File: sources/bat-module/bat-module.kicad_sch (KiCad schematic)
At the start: 31 parts, among them IC1 FDS6898AZ, IC2 DS2777G+

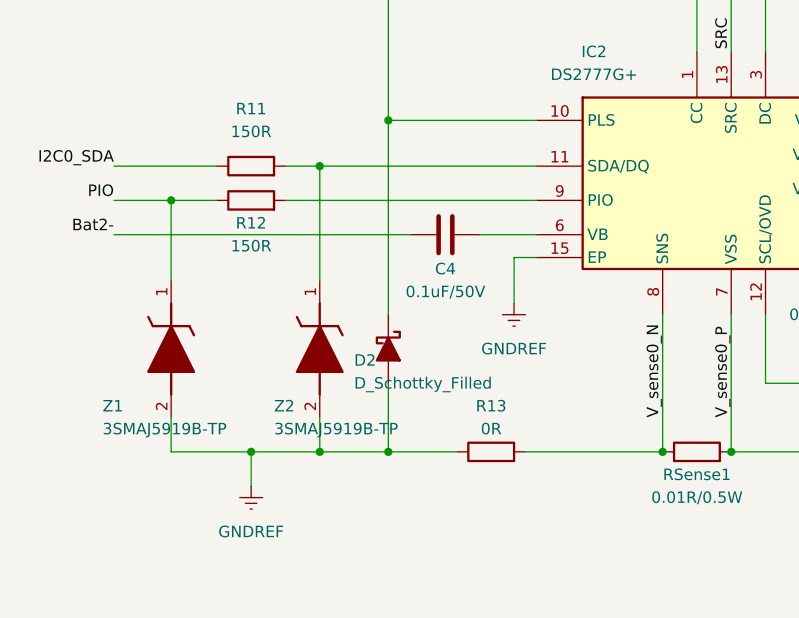
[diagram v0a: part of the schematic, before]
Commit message: hardware: creating batteries circuit
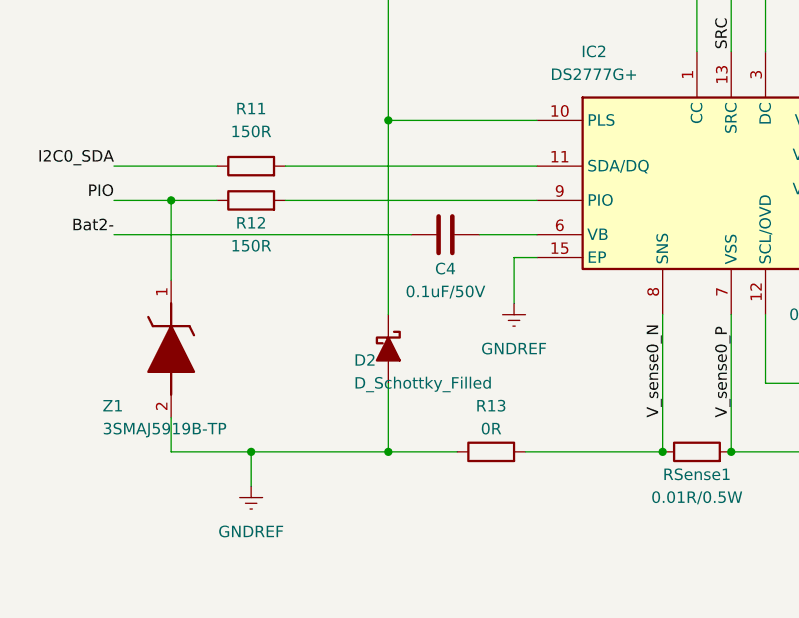
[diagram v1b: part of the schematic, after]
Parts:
- removed Z2: 3SMAJ5919B-TP, DIOM5226X244N, symbol 3SMAJ5919B-TP:3SMAJ5919B-TP
- IC1: footprint SOIC127P600X175-8N -> (none)
- IC2: footprint SON40P500X300X80-15N-D -> (none)
- Z1: footprint DIOM5226X244N -> (none)
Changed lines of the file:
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@@
   (junction (at 78.74 78.74) (diameter 0) (color 0 0 0 0)
   )
-  (junction (at 50.8 163.83) (diameter 0) (color 0 0 0 0)
-  )
   (junction (at 114.3 78.74) (diameter 0) (color 0 0 0 0)
   )
@@
   (junction (at 129.54 78.74) (diameter 0) (color 0 0 0 0)
   )
-  (junction (at 50.8 132.08) (diameter 0) (color 0 0 0 0)
-  )
   (junction (at 92.71 97.79) (diameter 0) (color 0 0 0 0)
   )
@@
     (stroke (width 0) (type default))
   )
-  (wire (pts (xy 58.42 163.83) (xy 50.8 163.83))
-    (stroke (width 0) (type default))
-  )
   (wire (pts (xy 74.93 127) (xy 58.42 127))
     (stroke (width 0) (type default))
@@
     (stroke (width 0) (type default))
   )
-  (wire (pts (xy 46.99 132.08) (xy 50.8 132.08))
+  (wire (pts (xy 46.99 132.08) (xy 74.93 132.08))
     (stroke (width 0) (type default))
   )
@@
     (stroke (width 0) (type default))
   )
-  (wire (pts (xy 50.8 132.08) (xy 74.93 132.08))
-    (stroke (width 0) (type default))
-  )
   (wire (pts (xy 68.58 139.7) (xy 74.93 139.7))
     (stroke (width 0) (type default))
@@
     (stroke (width 0) (type default))
   )
-  (wire (pts (xy 50.8 132.08) (xy 50.8 144.78))
-    (stroke (width 0) (type default))
-  )
   (wire (pts (xy 140.97 130.81) (xy 113.03 130.81))
     (stroke (width 0) (type default))
@@
     (stroke (width 0) (type default))
   )
-  (wire (pts (xy 50.8 163.83) (xy 43.18 163.83))
+  (wire (pts (xy 43.18 163.83) (xy 58.42 163.83))
     (stroke (width 0) (type default))
   )
@@
   )
   (wire (pts (xy 129.54 78.74) (xy 140.97 78.74))
-    (stroke (width 0) (type default))
-  )
-  (wire (pts (xy 50.8 160.02) (xy 50.8 163.83))
     (stroke (width 0) (type default))
   )
@@
       (effects (font (size 1.27 1.27)))
     )
-    (property "Footprint" "SON40P500X300X80-15N-D" (at 106.68 221.92 0)
+    (property "Footprint" "" (at 106.68 221.92 0)
       (effects (font (size 1.27 1.27)) (justify left top) hide)
     )
@@
       (effects (font (size 1.27 1.27)) (justify left))
     )
-    (property "Footprint" "DIOM5226X244N" (at -59.36 154.94 0)
+    (property "Footprint" "" (at -59.36 154.94 0)
       (effects (font (size 1.27 1.27)) (justify left top) hide)
     )
@@
       (effects (font (size 1.27 1.27)))
     )
-    (property "Footprint" "SOIC127P600X175-8N" (at 105.41 162.23 0)
+    (property "Footprint" "" (at 105.41 162.23 0)
       (effects (font (size 1.27 1.27)) (justify left top) hide)
     )
@@
         )
       )
-    )
-  )
-  (symbol (lib_id "3SMAJ5919B-TP:3SMAJ5919B-TP") (at 50.8 144.78 270) (unit 1)
-    (in_bom yes) (on_board yes) (dnp no)
-    (property "Reference" "Z2" (at 45.72 158.75 90)
-      (effects (font (size 1.27 1.27)) (justify left))
-    )
-    (property "Value" "3SMAJ5919B-TP" (at 45.72 161.29 90)
-      (effects (font (size 1.27 1.27)) (justify left))
-    )
-    (property "Footprint" "DIOM5226X244N" (at -42.85 154.94 0)
-      (effects (font (size 1.27 1.27)) (justify left top) hide)
-    )
-    (property "Datasheet" "https://mccsemi.com/pdf/Products/3SMAJ5918B-3SMAJ5956B(SMA).pdf" (at -142.85 154.94 0)
-      (effects (font (size 1.27 1.27)) (justify left top) hide)
-    )
-    (property "Height" "2.44" (at -342.85 154.94 0)
-      (effects (font (size 1.27 1.27)) (justify left top) hide)
-    )
-    (property "Mouser Part Number" "833-3SMAJ5919B-TP" (at -442.85 154.94 0)
-      (effects (font (size 1.27 1.27)) (justify left top) hide)
-    )
-    (property "Mouser Price/Stock" "https://www.mouser.co.uk/ProductDetail/Micro-Commercial-Components-MCC/3SMAJ5919B-TP?qs=ZNK0BnemlqFOug%252B1FuXOvQ%3D%3D" (at -542.85 154.94 0)
-      (effects (font (size 1.27 1.27)) (justify left top) hide)
-    )
-    (property "Manufacturer_Name" "MCC" (at -642.85 154.94 0)
-      (effects (font (size 1.27 1.27)) (justify left top) hide)
-    )
-    (property "Manufacturer_Part_Number" "3SMAJ5919B-TP" (at -742.85 154.94 0)
-      (effects (font (size 1.27 1.27)) (justify left top) hide)
-    )
-    (pin "1")
-    (pin "2")
-    (instances
-      (project "bat-module"
-        (path "/95270ebd-bf33-49a5-840f-dadc8a9f9793"
-          (reference "Z2") (unit 1)
-        )
-      )

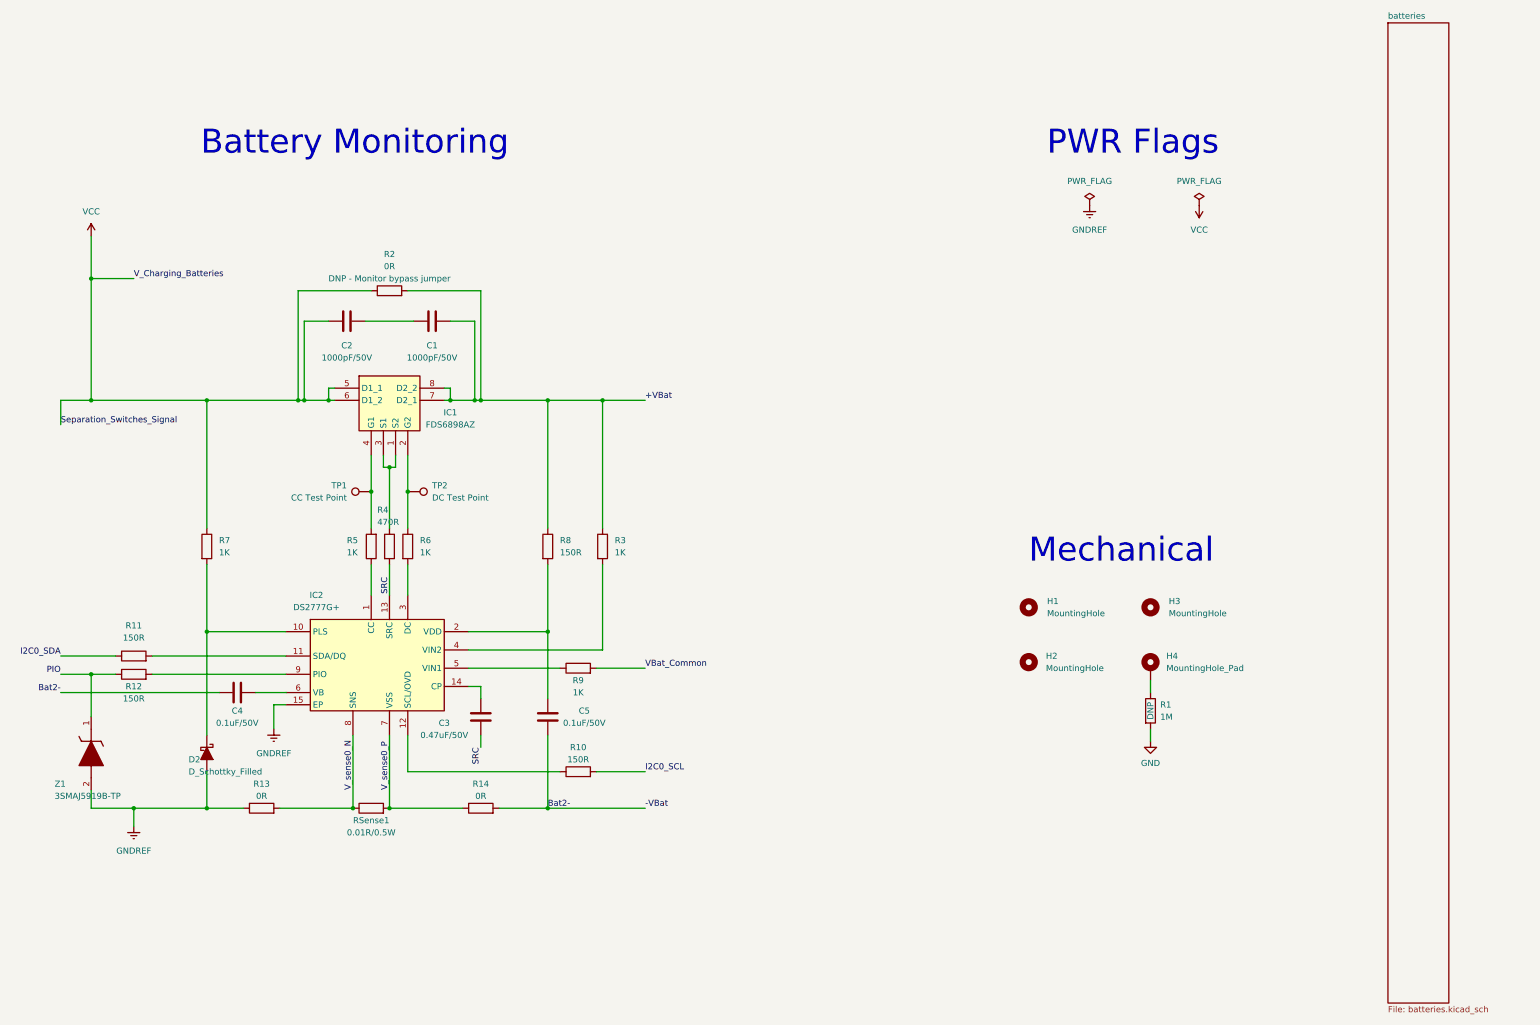
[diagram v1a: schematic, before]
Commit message: i2c-obdh connection and removing picoblade interface #3 #4
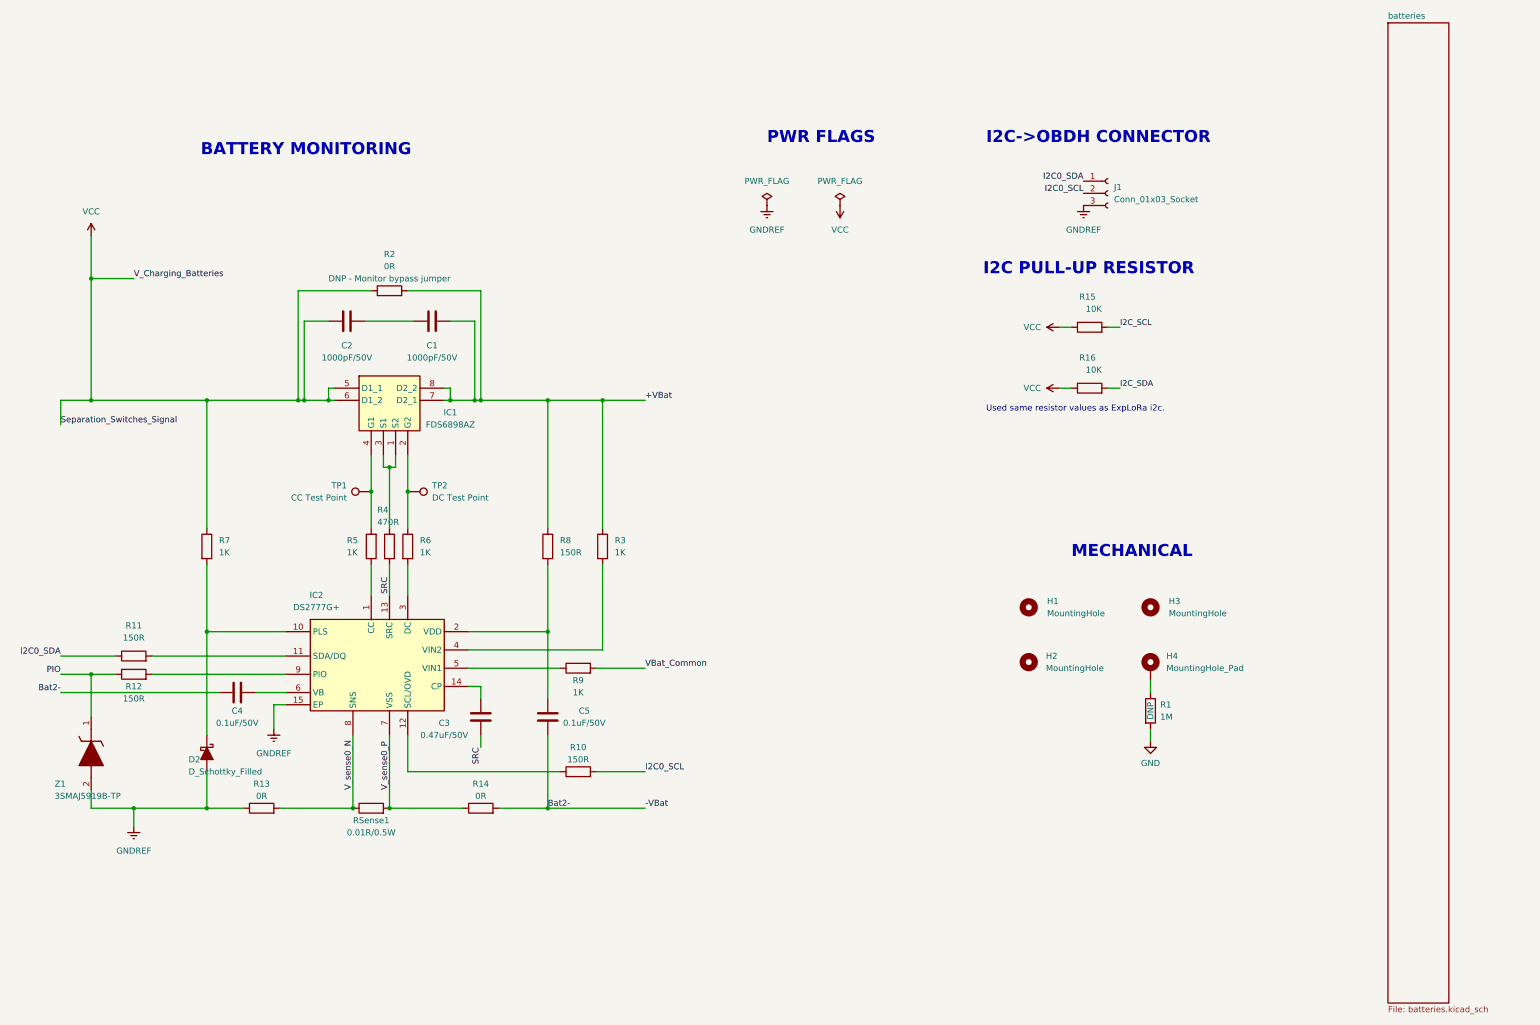
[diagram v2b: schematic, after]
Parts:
- added J1: Conn_01x03_Socket, symbol Connector:Conn_01x03_Socket
- added R15, R16: 10K, Resistor_SMD:R_0603_1608Metric_Pad0.98x0.95mm_HandSolder, symbol Device:R
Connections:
- net GNDREF: now also J1.3 (Pin_3)
- net I2C0_SCL: now also J1.2 (Pin_2)
- net I2C0_SDA: now also J1.1 (Pin_1)
- net VCC: now also R15.1, R16.1
- new net I2C_SCL: R15.2
- new net I2C_SDA: R16.2
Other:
- note added: "BATTERY MONITORING"
- note added: "I2C PULL-UP RESISTOR"
- note added: "I2C->OBDH CONNECTOR"
- note added: "MECHANICAL"
- note added: "PWR FLAGS"
- note added: "Used same resistor values as ExpLoRa i2c."
- note removed: "Battery Monitoring"
- note removed: "Mechanical"
- note removed: "PWR Flags"
